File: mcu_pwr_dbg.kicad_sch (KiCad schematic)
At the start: 6 parts, among them J8 Conn_ARM_JTAG_SWD_10, Y1 12M

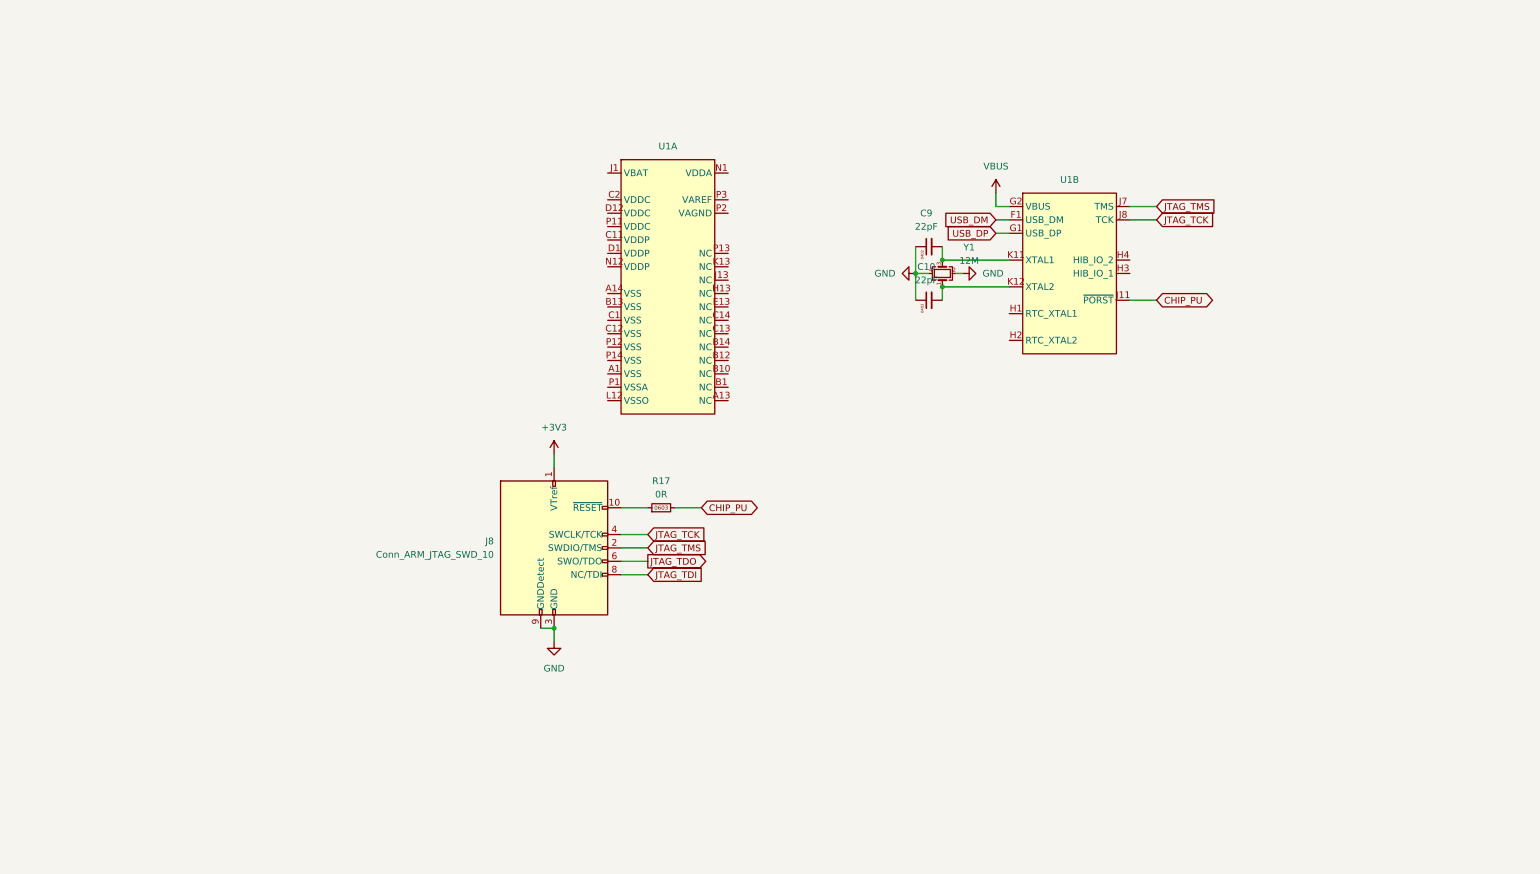
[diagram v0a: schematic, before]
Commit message: push forwards: clock muxing, filling in blanks
Finished off the ethernet section finally.
Sorted a solution to the 25M phy clocks required for ethercat
Connected CAN as per existing hardware (and fixed a bug in speed mode)
Sorted out bypassing for MCU
Added more thoughts on the external interfaces
Started on a 24V supply
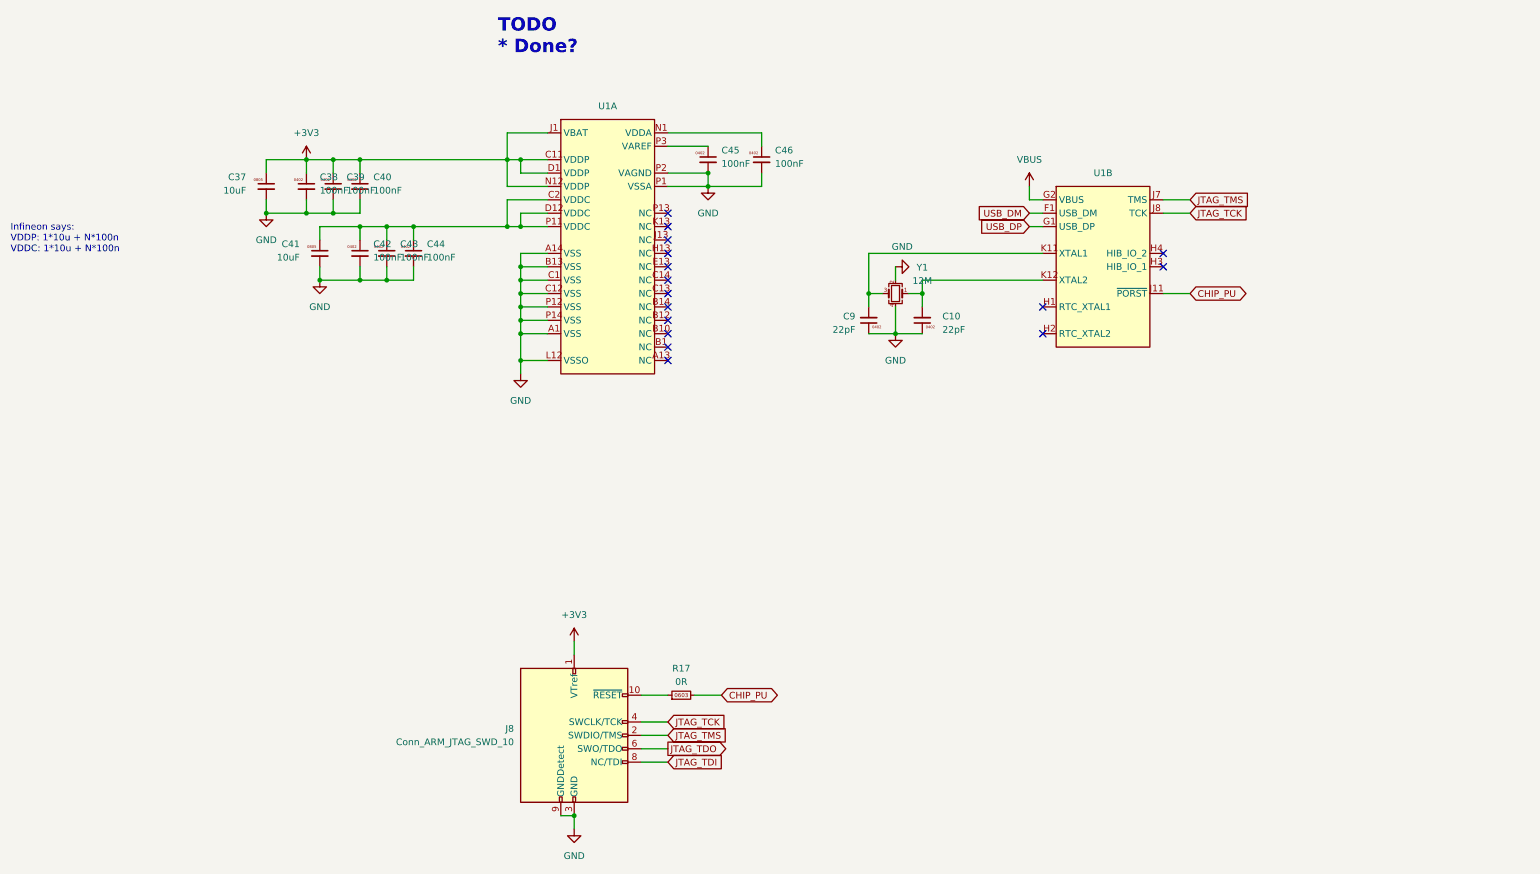
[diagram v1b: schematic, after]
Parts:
- added C37, C41: 10uF, Capacitor_SMD:C_0805_2012Metric, symbol karl-atomic-basic:KC0805_10uF_25V
- added C38, C39, C40, C42, C43, C44, C45, C46: 100nF, Capacitor_SMD:C_0402_1005Metric, symbol karl-atomic-basic:KC0402_100nF
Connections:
- net +3V3: now also U1.C11 (VDDP), U1.D1 (VDDP), U1.J1 (VBAT), U1.N12 (VDDP), C37.1, C38.1, C39.1, C40.1
- net GND: now also U1.A1 (VSS), U1.A14 (VSS), U1.B13 (VSS), U1.C1 (VSS), U1.C12 (VSS), U1.L12 (VSSO), U1.P1 (VSSA), U1.P12 (VSS), U1.P14 (VSS), U1.P2 (VAGND), C37.2, C38.2, C39.2, C40.2, C41.2, C42.2, C43.2, C44.2, C45.2, C46.2
- net at U1.C2 (VDDC): now also U1.D12 (VDDC), U1.P11 (VDDC), C41.1, C42.1, C43.1, C44.1
- net at U1.N1 (VDDA): now also C46.1
- net at U1.P3 (VAREF): now also C45.1
- no-connect marks 0 -> 16
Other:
- note added: "Infineon says: VDDP: 1*10u + N*100n VDDC: 1*10u + N*100n"
- note added: "TODO * Done?"
- moved on the sheet: C10, C9, J8, R17, U1A, U1B, Y1

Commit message: sch: clean up layout a little
just make it prettier
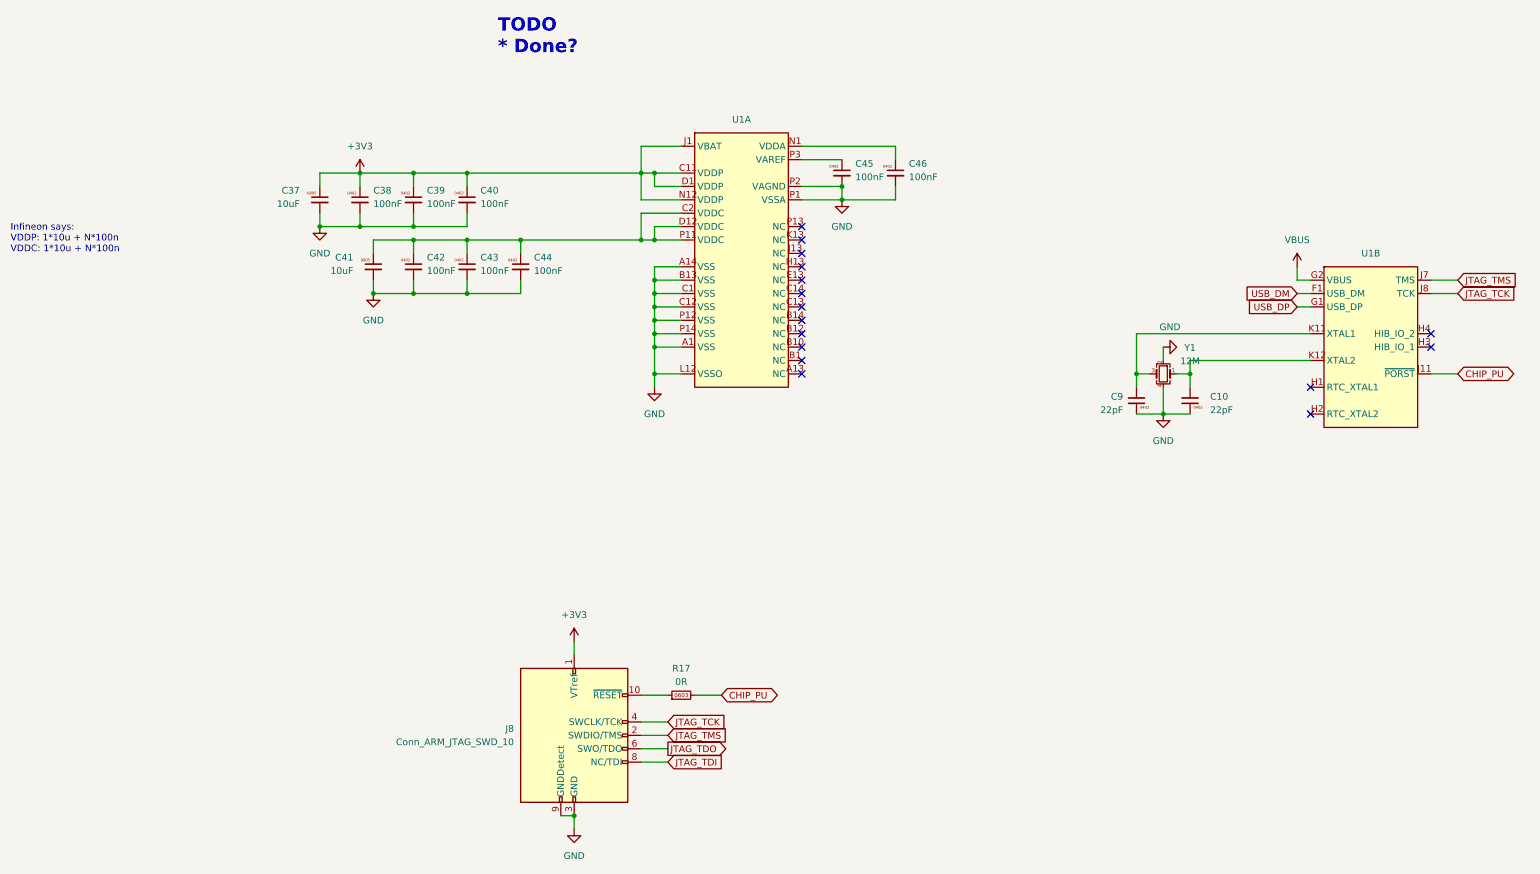
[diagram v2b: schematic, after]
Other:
- moved on the sheet: C10, C37, C38, C39, C40, C41, C42, C43, C44, C45, C46, C9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

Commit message: finish a 24V supply
went with a more modern one, plenty of room.  Should be pretty good now.
Went over and filled in a bunch of missing parts and things, cleaned up
as much as I could 0603 vs 0402 for most, updated some thigns to current
atomic part library.

still to go, the "pi" interface and some sort of spi/io interface?
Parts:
- R17: jlcbasic (none) -> basic
- U1: value (none) -> XMC4800-E196
